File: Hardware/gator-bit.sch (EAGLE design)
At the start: 84 parts, among them J1 GATOR, J19 GATOR, J2 GATOR, J20 GATOR, J21 GATOR, J22 GATOR, J25 GATOR, J28 GATOR, J3 GATOR, J32 GATOR, J33 GATOR, J34 GATOR, J35 GATOR, J36 GATOR, J39 GATOR, J4 GATOR, J40 GATOR, J42 GATOR, U1 5V, U2 micro:bit, U4 MIC5219 3.3V

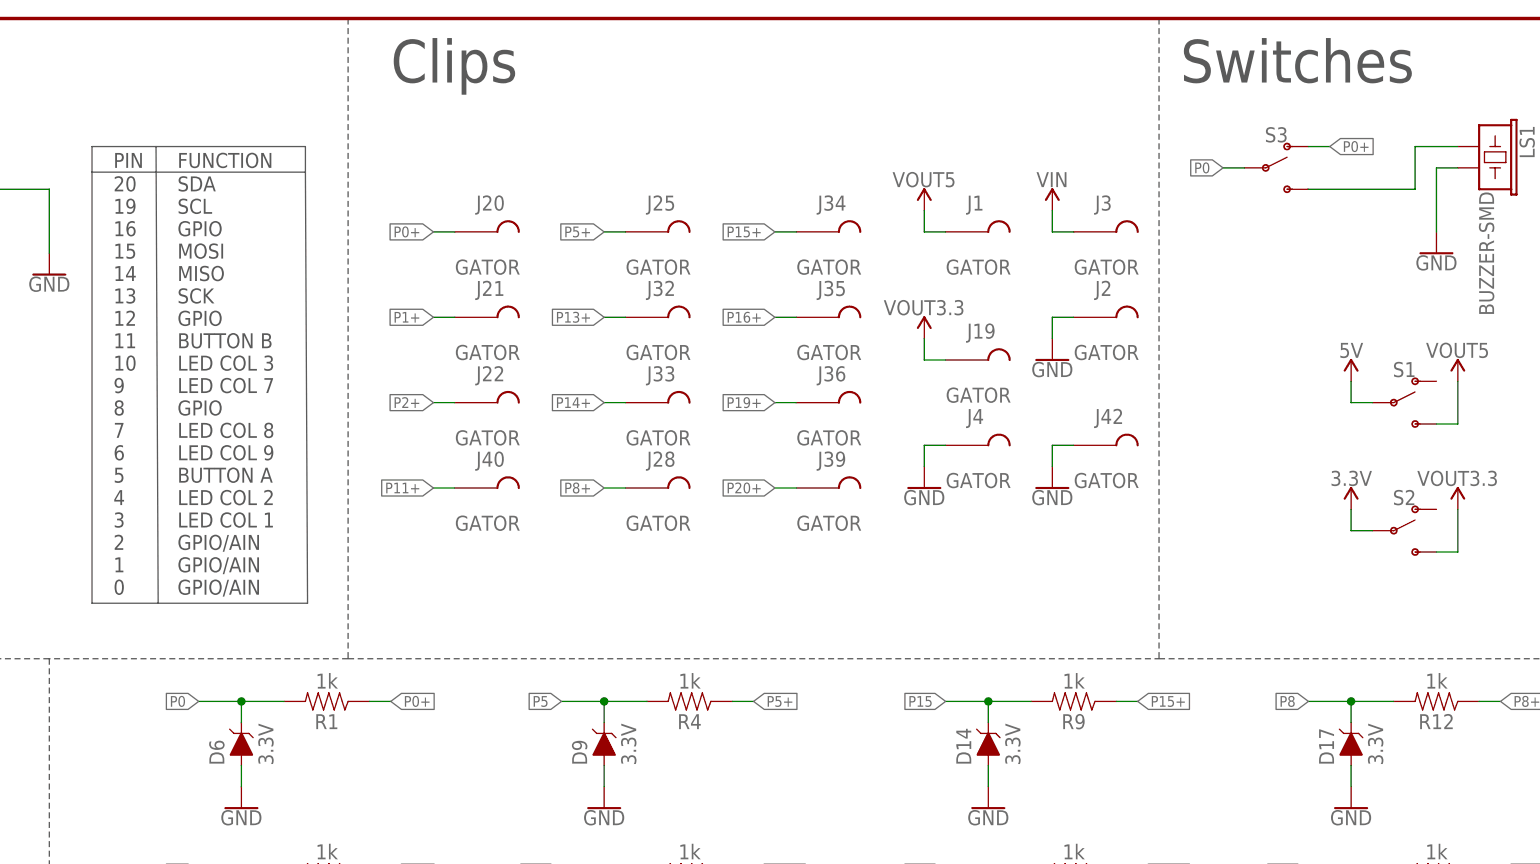
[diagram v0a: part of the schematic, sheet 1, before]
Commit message: Updating BRD and SCH files -fixed switch problem - isolate speaker and protected pin 0 line -Added silk labels to GPIO -Aesthetics on SCH
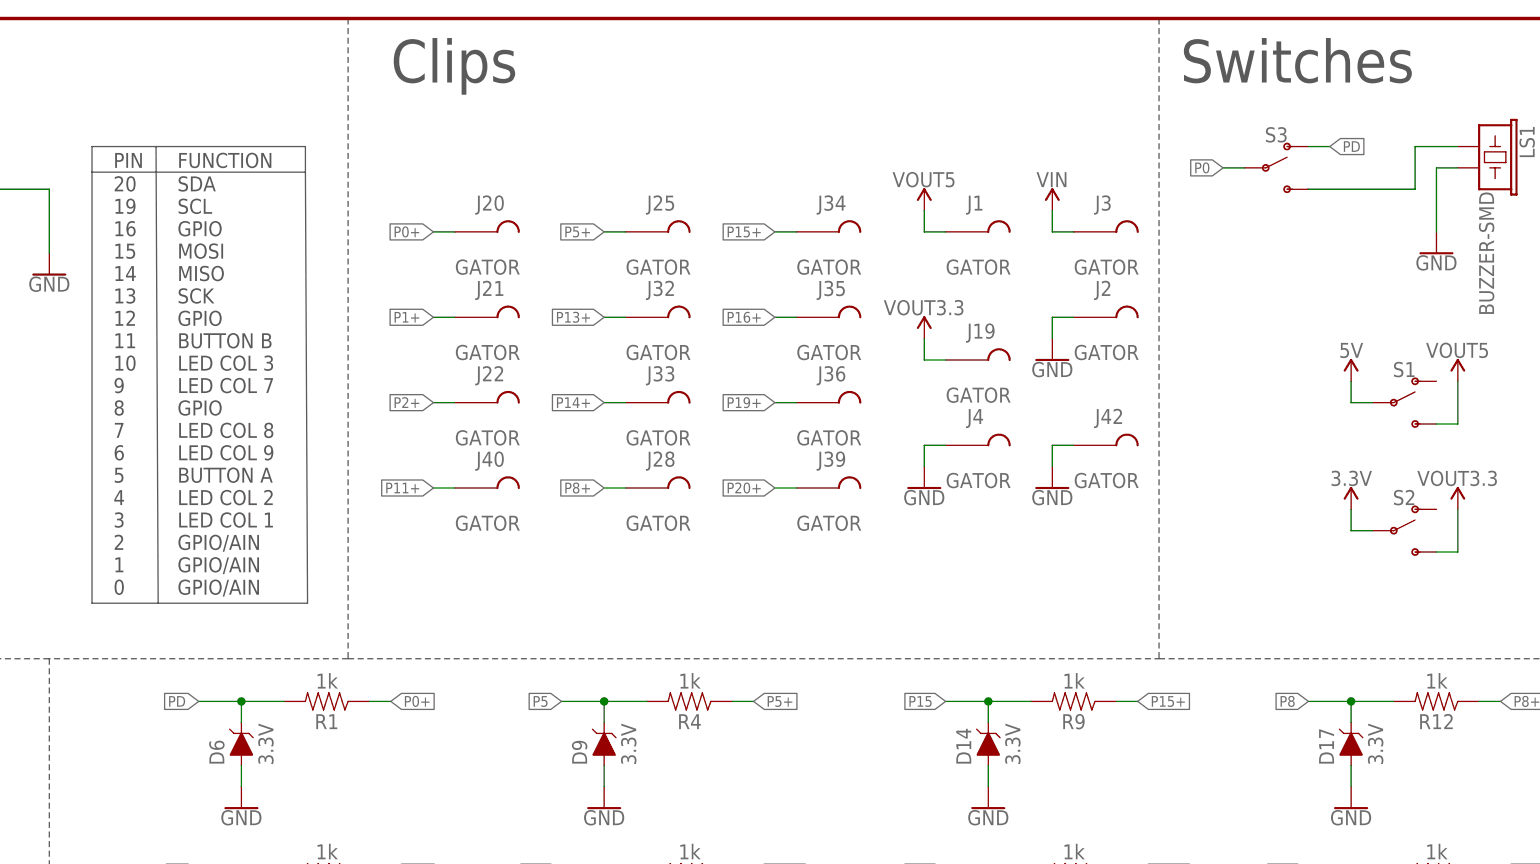
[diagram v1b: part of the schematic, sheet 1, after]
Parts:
- LOGO1: value SFE_LOGO_FLAME.2_INCH -> SFE_LOGO_FLAME.3_INCH; device SparkFun-Aesthetics:SFE_LOGO_FLAME.2_INCH -> SparkFun-Aesthetics:SFE_LOGO_FLAME.3_INCH
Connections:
- new net PD: D6.C, R1.2, S3.O
- net P0: no longer D6.C, R1.2
- net P0+: no longer S3.O
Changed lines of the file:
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@@
 <part name="GND3" library="SparkFun-PowerSymbols" deviceset="GND" device=""/>
 <part name="SUPPLY4" library="SparkFun-PowerSymbols" deviceset="VIN" device=""/>
-<part name="LOGO1" library="SparkFun-Aesthetics" deviceset="SFE_LOGO_FLAME" device=".2_INCH"/>
+<part name="LOGO1" library="SparkFun-Aesthetics" deviceset="SFE_LOGO_FLAME" device=".3_INCH" value="SFE_LOGO_FLAME.3_INCH"/>
 <part name="LS1" library="SparkFun-Electromechanical" deviceset="BUZZER" device="-SMD"/>
 <part name="S1" library="SparkFun-Switches" deviceset="SWITCH-SPDT" device="-SMD-AYZ0202"/>
@@
 <label x="205.74" y="167.64" size="1.27" layer="95" font="vector" rot="R180" xref="yes"/>
 </segment>
-<segment>
-<pinref part="R1" gate="G$1" pin="2"/>
-<wire x1="93.98" y1="104.14" x2="88.9" y2="104.14" width="0.1524" layer="91"/>
-<pinref part="D6" gate="G$1" pin="C"/>
-<wire x1="88.9" y1="104.14" x2="83.82" y2="104.14" width="0.1524" layer="91"/>
-<wire x1="88.9" y1="101.6" x2="88.9" y2="104.14" width="0.1524" layer="91"/>
-<junction x="88.9" y="104.14"/>
-<label x="83.82" y="104.14" size="1.27" layer="95" font="vector" rot="R180" xref="yes"/>
-</segment>
 </net>
 <net name="P1" class="0">
@@
 </segment>
 <segment>
-<pinref part="S3" gate="1" pin="O"/>
-<wire x1="215.9" y1="170.18" x2="218.44" y2="170.18" width="0.1524" layer="91"/>
-<label x="218.44" y="170.18" size="1.27" layer="95" font="vector" xref="yes"/>
-</segment>
-<segment>
 <pinref part="R1" gate="G$1" pin="1"/>
 <wire x1="104.14" y1="104.14" x2="106.68" y2="104.14" width="0.1524" layer="91"/>
@@
 </segment>
 </net>
+<net name="PD" class="0">
+<segment>
+<pinref part="R1" gate="G$1" pin="2"/>
+<wire x1="93.98" y1="104.14" x2="88.9" y2="104.14" width="0.1524" layer="91"/>
+<pinref part="D6" gate="G$1" pin="C"/>
+<wire x1="88.9" y1="104.14" x2="83.82" y2="104.14" width="0.1524" layer="91"/>
+<wire x1="88.9" y1="101.6" x2="88.9" y2="104.14" width="0.1524" layer="91"/>
+<junction x="88.9" y="104.14"/>
+<label x="83.82" y="104.14" size="1.27" layer="95" font="vector" rot="R180" xref="yes"/>
+</segment>
+<segment>
+<pinref part="S3" gate="1" pin="O"/>
+<wire x1="215.9" y1="170.18" x2="218.44" y2="170.18" width="0.1524" layer="91"/>
+<label x="218.44" y="170.18" size="1.27" layer="95" font="vector" xref="yes"/>
+</segment>
+</net>

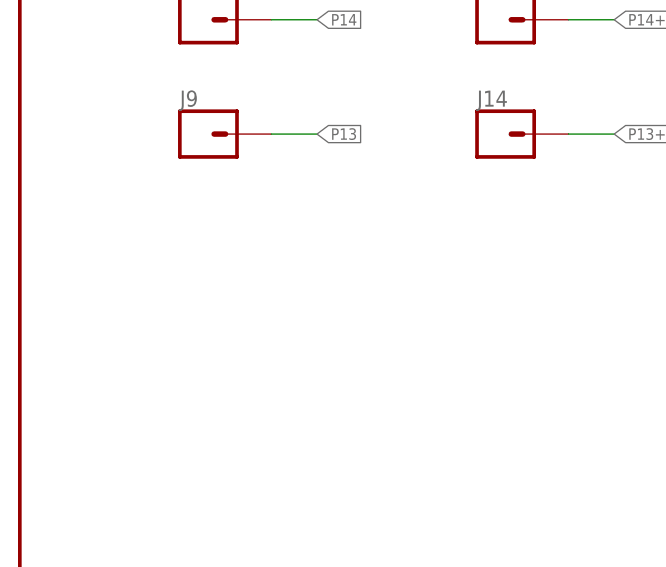
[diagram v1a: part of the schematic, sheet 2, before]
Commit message: Added a battery connector
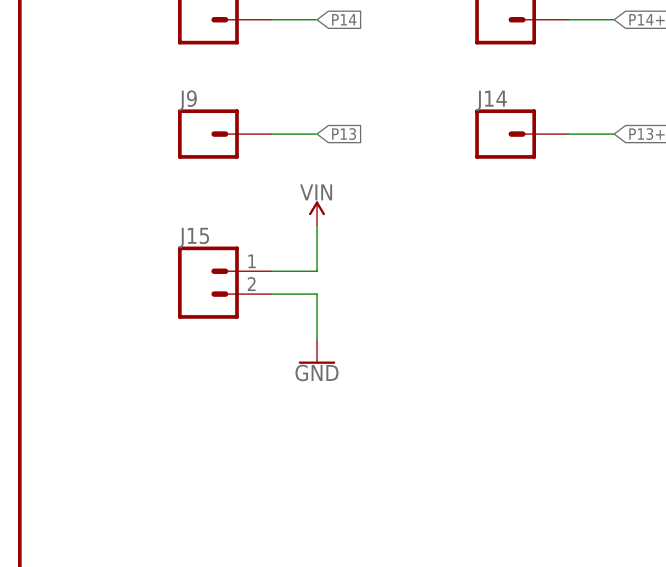
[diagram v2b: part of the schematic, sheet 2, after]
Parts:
- added J15: (no value), SparkFun-Connectors:CONN_02-JST-2MM-SMT
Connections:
- net GND: now also J15.1
- net VIN: now also J15.2
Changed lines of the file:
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@@
 <part name="GND24" library="SparkFun-PowerSymbols" deviceset="GND" device=""/>
 <part name="GND25" library="SparkFun-PowerSymbols" deviceset="GND" device=""/>
+<part name="J15" library="SparkFun-Connectors" deviceset="CONN_02" device="-JST-2MM-SMT"/>
+<part name="SUPPLY6" library="SparkFun-PowerSymbols" deviceset="VIN" device=""/>
+<part name="GND26" library="SparkFun-PowerSymbols" deviceset="GND" device=""/>
 </parts>
 <sheets>
@@
 <instance part="GND24" gate="1" x="106.68" y="147.32"/>
 <instance part="GND25" gate="1" x="116.84" y="147.32"/>
+<instance part="J15" gate="G$1" x="20.32" y="45.72"/>
+<instance part="SUPPLY6" gate="G$1" x="33.02" y="53.34"/>
+<instance part="GND26" gate="1" x="33.02" y="38.1"/>
 </instances>
 <busses>
@@
 <pinref part="GND25" gate="1" pin="GND"/>
 <wire x1="116.84" y1="152.4" x2="116.84" y2="149.86" width="0.1524" layer="91"/>
+</segment>
+<segment>
+<pinref part="J15" gate="G$1" pin="1"/>
+<wire x1="27.94" y1="45.72" x2="33.02" y2="45.72" width="0.1524" layer="91"/>
+<wire x1="33.02" y1="45.72" x2="33.02" y2="40.64" width="0.1524" layer="91"/>
+<pinref part="GND26" gate="1" pin="GND"/>
 </segment>
 </net>
@@
 <pinref part="SUPPLY5" gate="G$1" pin="VIN"/>
 </segment>
-</net>
+<segment>
+<pinref part="J15" gate="G$1" pin="2"/>
+<wire x1="27.94" y1="48.26" x2="33.02" y2="48.26" width="0.1524" layer="91"/>
+<wire x1="33.02" y1="48.26" x2="33.02" y2="53.34" width="0.1524" layer="91"/>
+<pinref part="SUPPLY6" gate="G$1" pin="VIN"/>
+</segment>
+</net>

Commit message: Updated design
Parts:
- removed C6: 10uF, SparkFun-Capacitors:10UF-POLAR-0603-6.3V-20%(TANT)
- removed J1, J42: GATOR, TAB:GATOR
- removed S1: (no value), SparkFun-Switches:SWITCH-SPDT-SMD-AYZ0202
- removed U1: 5V, SparkFun-IC-Power:V_REG_MIC52055V
- added S4: (no value), SparkFun-Switches:SWITCH-SPDT-SMD-AYZ0202
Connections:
- removed net 5V: C1.2, C2.2, C3.2, C4.2, C5.2, C6.+, D1.VDD, D2.VDD, D3.VDD, D4.VDD, D5.VDD, S1.P, U1.OUT
- removed net VOUT5: J1.P$1, S1.S
- new net VIN_TAB: J3.P$1, S4.O
- new net V_BATT: J15.2, S4.S
- net 3.3V: now also C1.2, C2.2, C3.2, C4.2, C5.2, D1.VDD, D2.VDD, D3.VDD, D4.VDD, D5.VDD
- net GND: no longer C6.-, J42.P$1, U1.GND
- net VIN: now also S4.P; no longer J15.2, J3.P$1, U1.EN, U1.IN
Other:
- note added: "3.3V Rail"
- note added: "If a LiPo battery is used only use the 3.3V Rail."
- moved on the sheet: C7, C8, C9, J15, U4

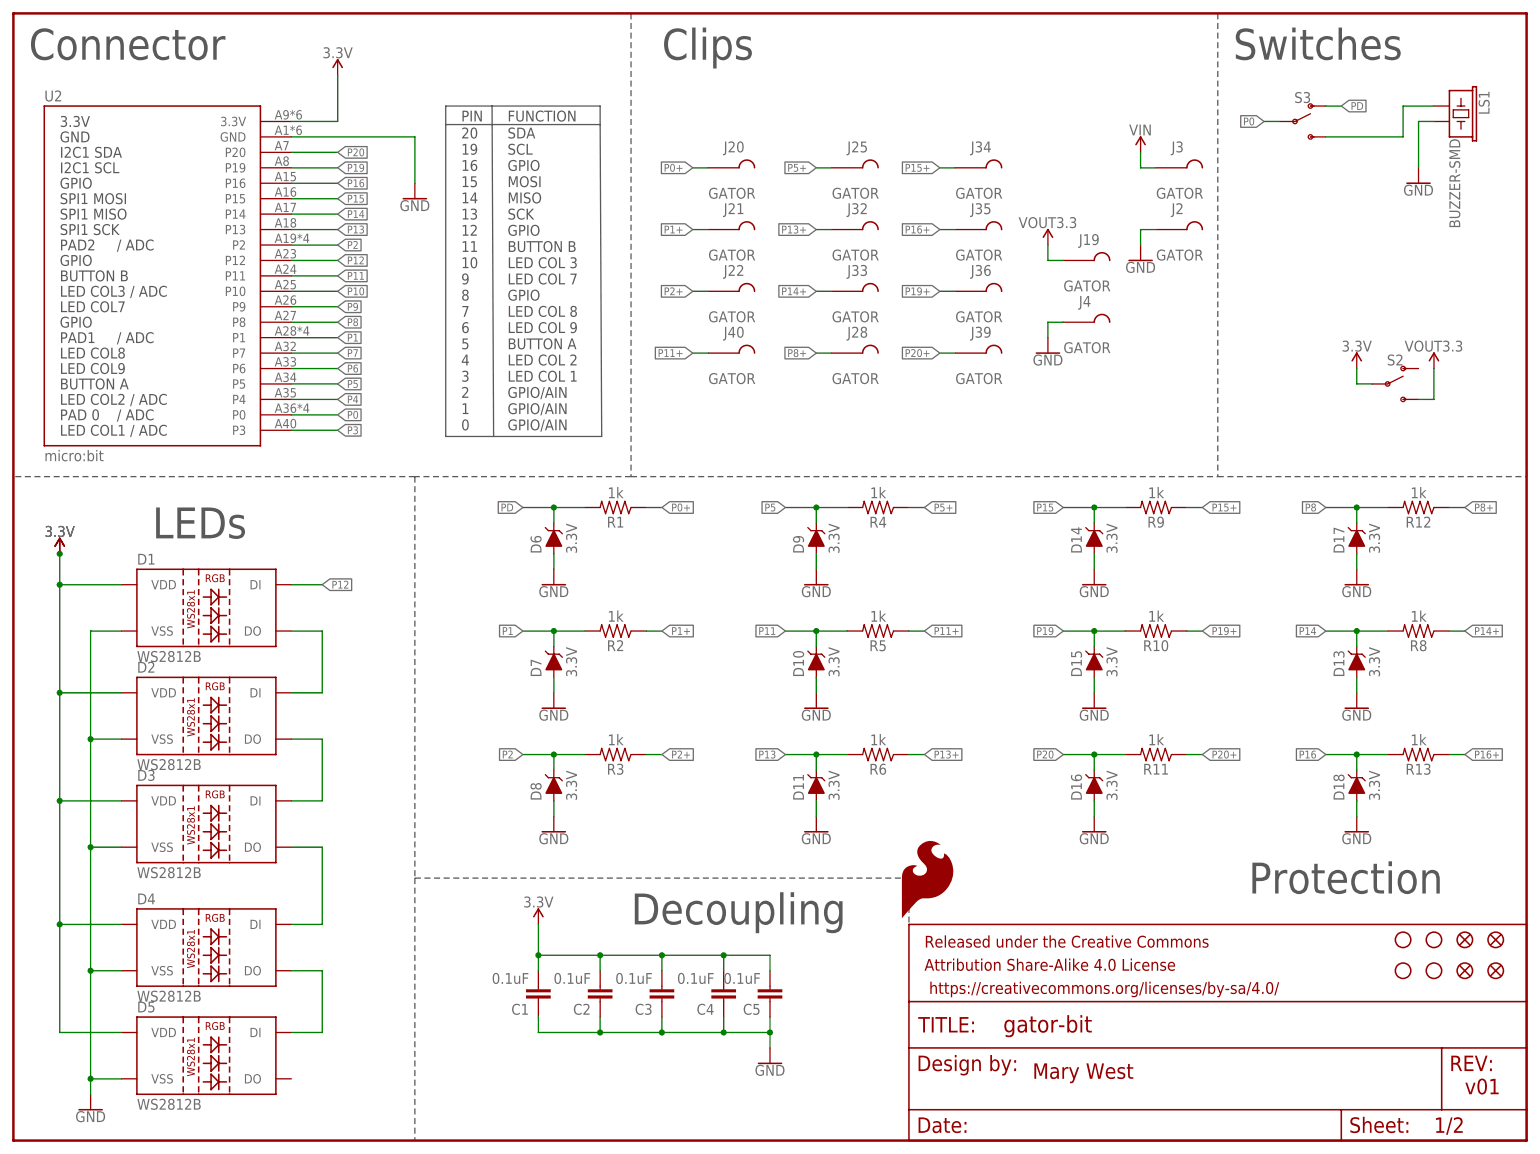
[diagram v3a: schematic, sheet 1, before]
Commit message: adding OSHW logo, VIN range note
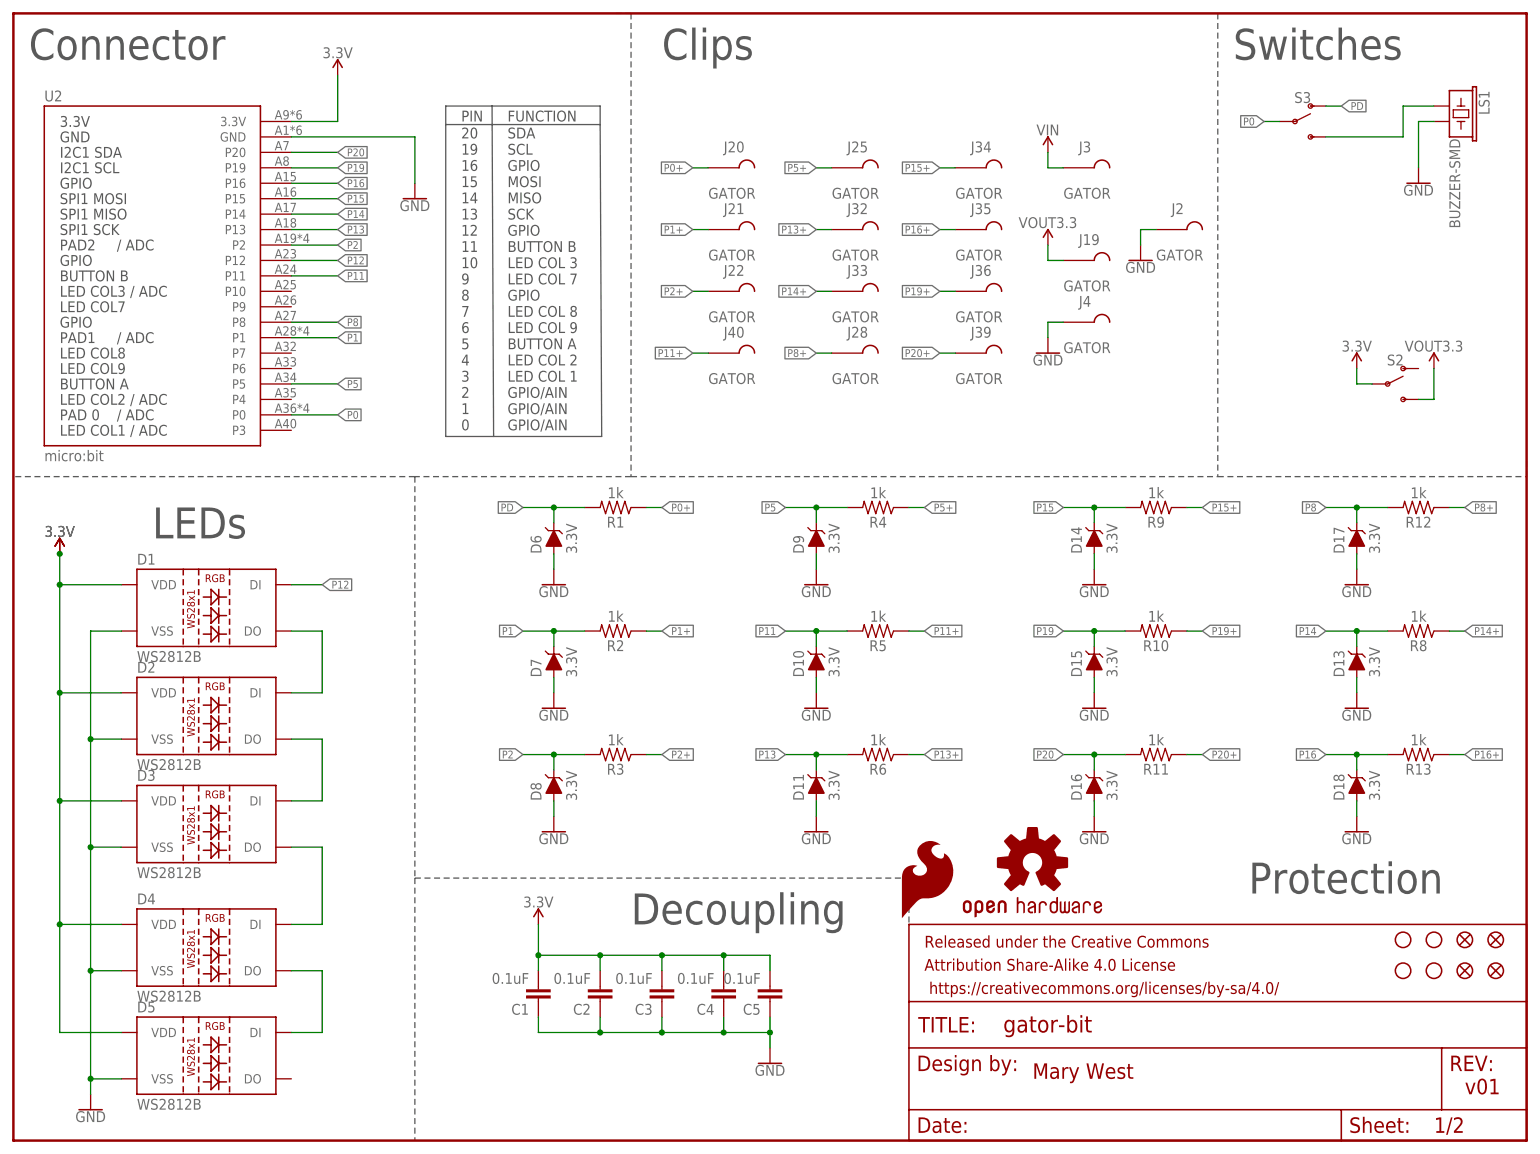
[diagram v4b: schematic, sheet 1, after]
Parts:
- added LOGO2: OSHW-LOGOM, SparkFun-Aesthetics:OSHW-LOGOM
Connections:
- removed net P10: U2.P10
- removed net P3: U2.P3
- removed net P4: U2.P4
- removed net P6: U2.P6
- removed net P7: U2.P7
- removed net P9: U2.P9
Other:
- note added: "VIN 3V-12V"
- note removed: "Power"
- moved on the sheet: C7, C8, C9, J10, J11, J12, J13, J14, J15, J3, J5, J6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
